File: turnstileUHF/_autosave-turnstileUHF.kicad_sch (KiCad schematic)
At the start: 57 parts, among them J1 Conn_Coaxial, J2 Conn_Coaxial, J3 Conn_Coaxial, J4 Conn_Coaxial, Q1 2N7002, Q2 2N7002, Q3 2N7002, Q4 2N7002, Q5 AO3401A, Q6 AO3401A, Q7 AO3401A, Q8 2N7002, SW1 SW_DIP_x04

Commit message: added trace antennas with coax links
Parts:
- ANT1, ANT2, ANT3, ANT4: footprint (none) -> RF_Antenna:Coilcraft_MA5532-AE_RFID
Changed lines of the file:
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@@
 			)
 		)
-		(property "Footprint" ""
+		(property "Footprint" "RF_Antenna:Coilcraft_MA5532-AE_RFID"
 			(at 196.85 130.81 0)
 			(hide yes)
@@
 			)
 		)
-		(property "Footprint" ""
+		(property "Footprint" "RF_Antenna:Coilcraft_MA5532-AE_RFID"
 			(at 255.27 129.54 0)
 			(hide yes)
@@
 			)
 		)
-		(property "Footprint" ""
+		(property "Footprint" "RF_Antenna:Coilcraft_MA5532-AE_RFID"
 			(at 171.45 130.81 0)
 			(hide yes)
@@
 			)
 		)
-		(property "Footprint" ""
+		(property "Footprint" "RF_Antenna:Coilcraft_MA5532-AE_RFID"
 			(at 228.6 130.81 0)
 			(hide yes)

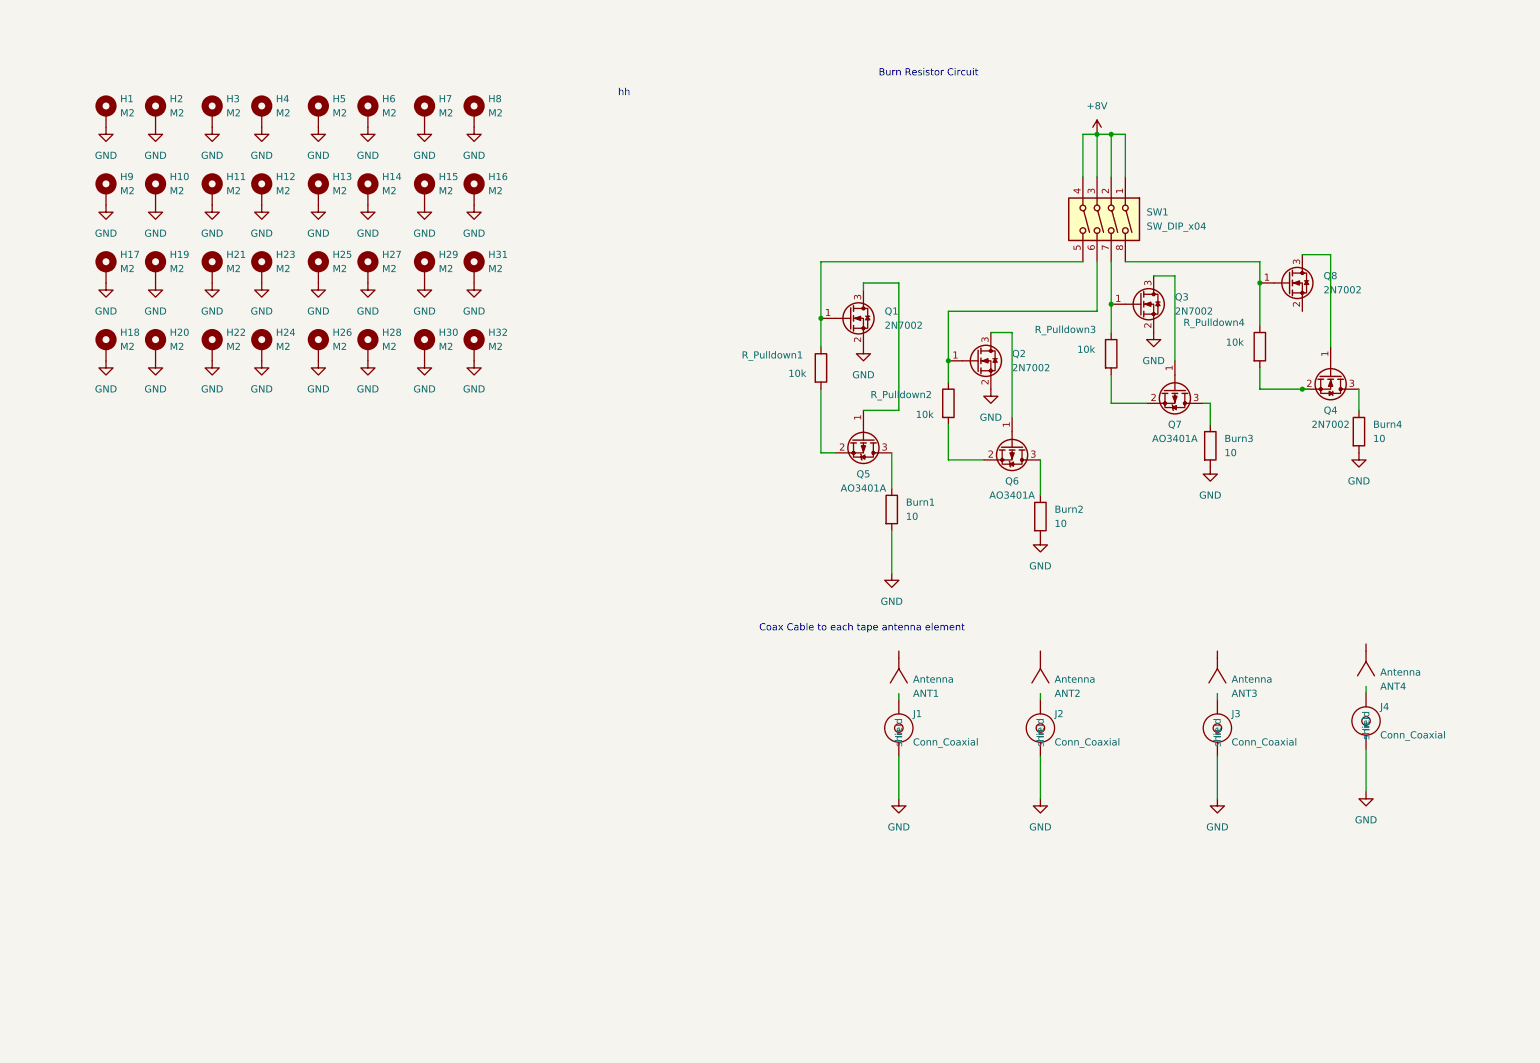
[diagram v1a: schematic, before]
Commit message: upated burn wire routing
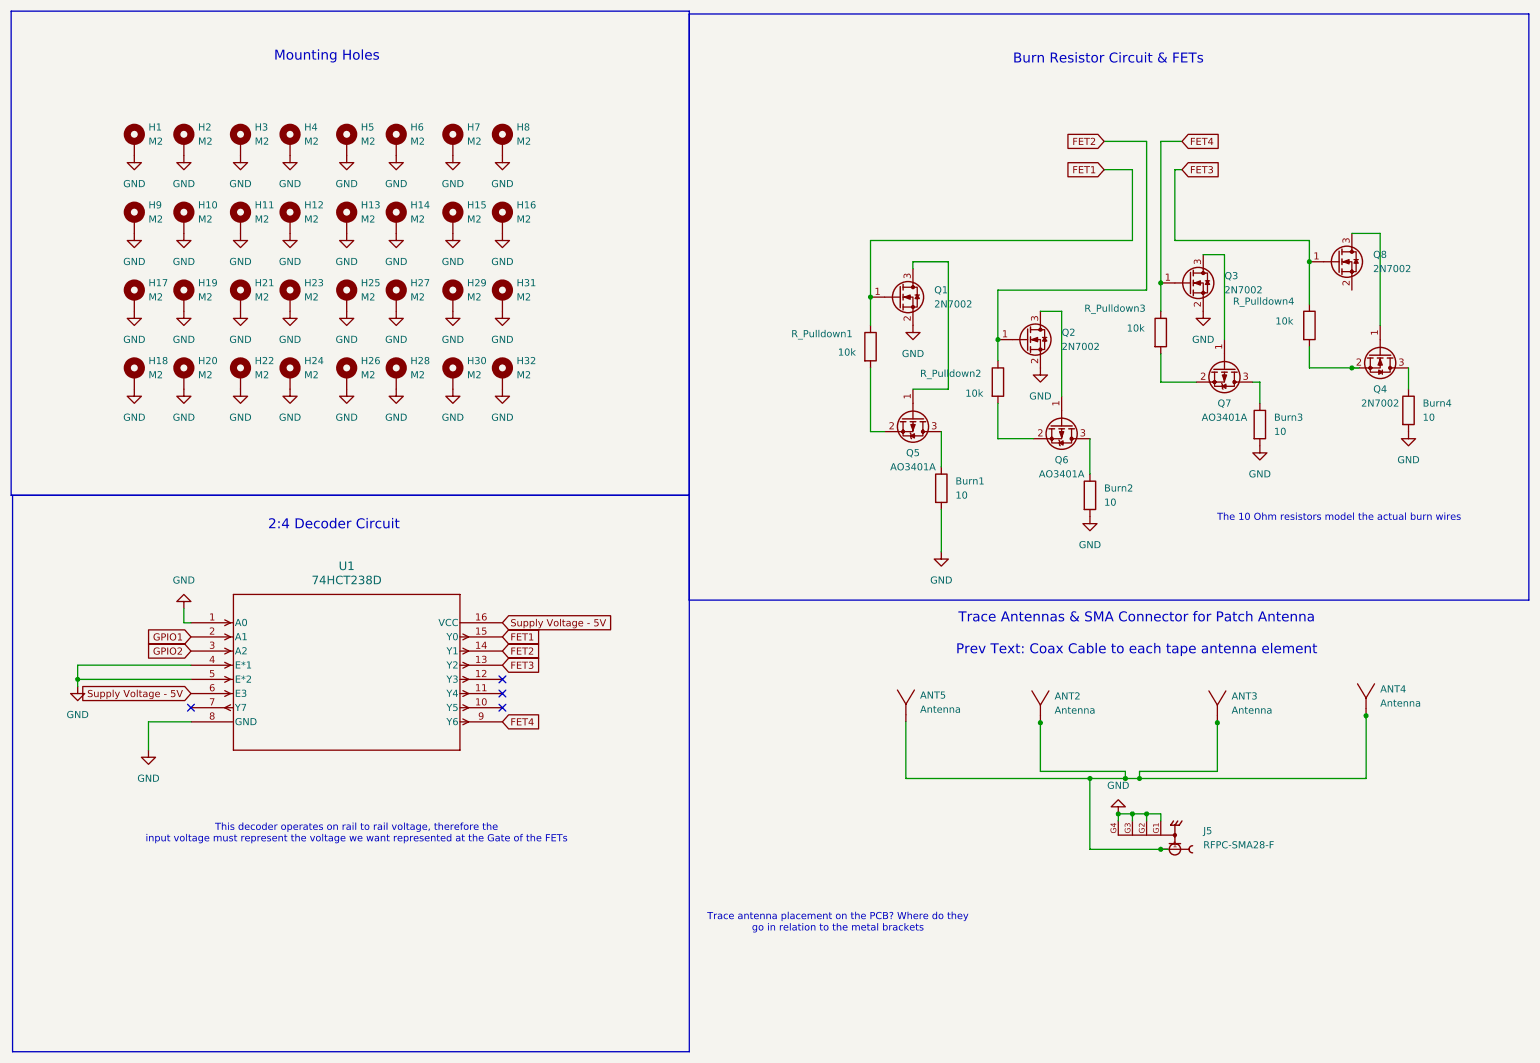
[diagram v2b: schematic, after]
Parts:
- removed ANT1: Antenna, RF_Antenna:Coilcraft_MA5532-AE_RFID, symbol Device:Antenna
- removed J1, J2, J3, J4: Conn_Coaxial, Connector_Coaxial:U.FL_Hirose_U.FL-R-SMT-1_Vertical, symbol Connector:Conn_Coaxial
- removed SW1: SW_DIP_x04, Button_Switch_SMD:SW_DIP_SPSTx04_Slide_6.7x11.72mm_W8.61mm_P2.54mm_LowProfile, symbol Switch:SW_DIP_x04
- added ANT5: Antenna, symbol Device:Antenna
- added J5: RFPC-SMA28-F, inspireFly:GRADCONN_RFPC-SMA28-F, symbol inspireFly:RFPC-SMA28-F
- added U1: 74HCT238D, inspireFly:SOT109-1_NXP, symbol inspireFly:74HCT238D
- ANT2, ANT3, ANT4: footprint RF_Antenna:Coilcraft_MA5532-AE_RFID -> (none)
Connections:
- net GND: now also J5.G1, J5.G2, J5.G3, J5.G4, U1.1 (A0), U1.4 (E*1), U1.5 (E*2), U1.8 (GND)
- net FET1: now reaches Q1.1 (G), R_Pulldown1.1
- net FET1: now also U1.15 (Y0)
- net at ANT2.1: now also ANT3.1, ANT4.1, ANT5.1, J5.1
- net FET4: now reaches Q3.1 (G), R_Pulldown3.1
- net FET4: now also U1.9 (Y6)
- net FET2: now reaches Q2.1 (G), R_Pulldown2.1
- net FET2: now also U1.14 (Y1)
- net FET3: now reaches Q8.1 (G), R_Pulldown4.1
- net FET3: now also U1.13 (Y2)
- new net GPIO1: U1.2 (A1)
- new net GPIO2: U1.3 (A2)
- new net Supply Voltage - 5V: U1.16 (VCC), U1.6 (E3)
- no-connect marks 0 -> 4
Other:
- note added: "2:4 Decoder Circuit"
- note added: "Burn Resistor Circuit & FETs"
- note added: "Mounting Holes"
- note added: "The 10 Ohm resistors model the actual burn wires"
- note added: "This decoder operates on rail to rail voltage, therefore the input voltage must represent the voltage we want represented at the Gate of the FETs"
- note added: "Trace Antennas & SMA Connector for Patch Antenna Prev Text: Coax Cable to each tape antenna element"
- note added: "Trace antenna placement on the PCB? Where do they go in relation to the metal brackets"
- note removed: "Burn Resistor Circuit"
- note removed: "Coax Cable to each tape antenna element"
- note removed: "hh"
- moved on the sheet: ANT2, ANT3, ANT4, Burn1, Burn2, Burn3, Burn4, H1, H10, H11, H12, H13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

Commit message: fixed missing antenna
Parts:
- ANT1: renamed from ANT5; footprint (none) -> RF_Antenna:Coilcraft_MA5532-AE_RFID
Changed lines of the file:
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@@
 		(dnp no)
 		(fields_autoplaced yes)
-		(property "Reference" "ANT5"
+		(property "Reference" "ANT1"
 			(at 175.26 134.9374 0)
 			(show_name no)
@@
 			)
 		)
-		(property "Footprint" ""
+		(property "Footprint" "RF_Antenna:Coilcraft_MA5532-AE_RFID"
 			(at 172.72 135.89 0)
 			(hide yes)
@@
 			(project "turnstileUHF"
 				(path "/bb80e4f3-3333-4302-bfd1-5248f999de56"
-					(reference "ANT5")
+					(reference "ANT1")
 					(unit 1)
 				)
